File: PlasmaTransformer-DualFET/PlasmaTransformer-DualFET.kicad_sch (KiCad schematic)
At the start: 51 parts, among them J1 Barrel_Jack_MountingPin, J10 Screw_Terminal_01x01, J11 Screw_Terminal_01x01, J12 Screw_Terminal_01x01, J2 Conn_01x02_Pin, J3 Conn_Coaxial, J4 Conn_02x04_Odd_Even, J5 Conn_Coaxial, J6 Screw_Terminal_01x01, J7 Screw_Terminal_01x01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

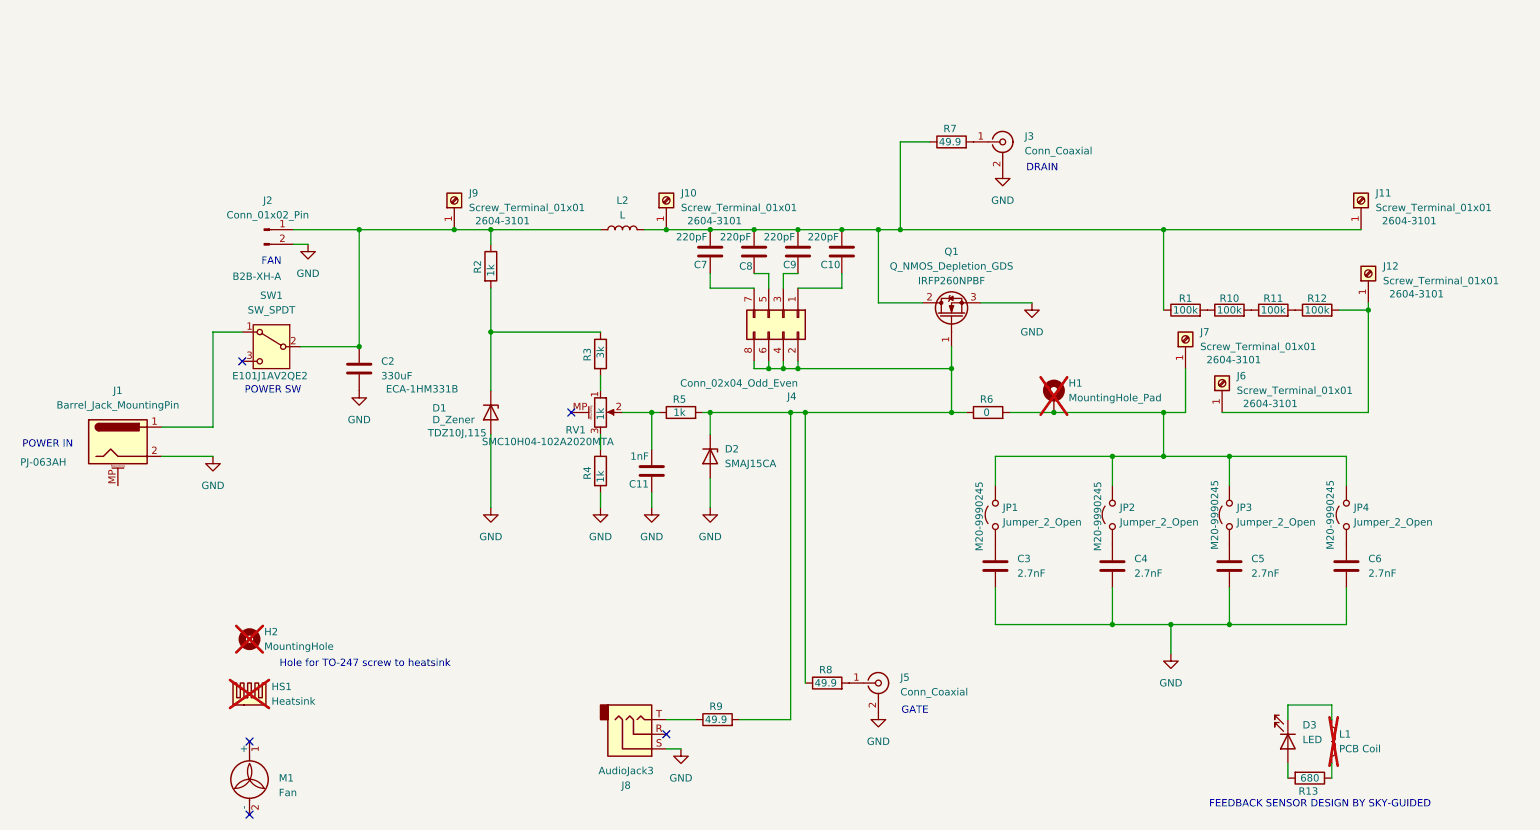
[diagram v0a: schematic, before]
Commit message: Updated rev 2 design and manufacturing files.  Note BOM is not up to date.
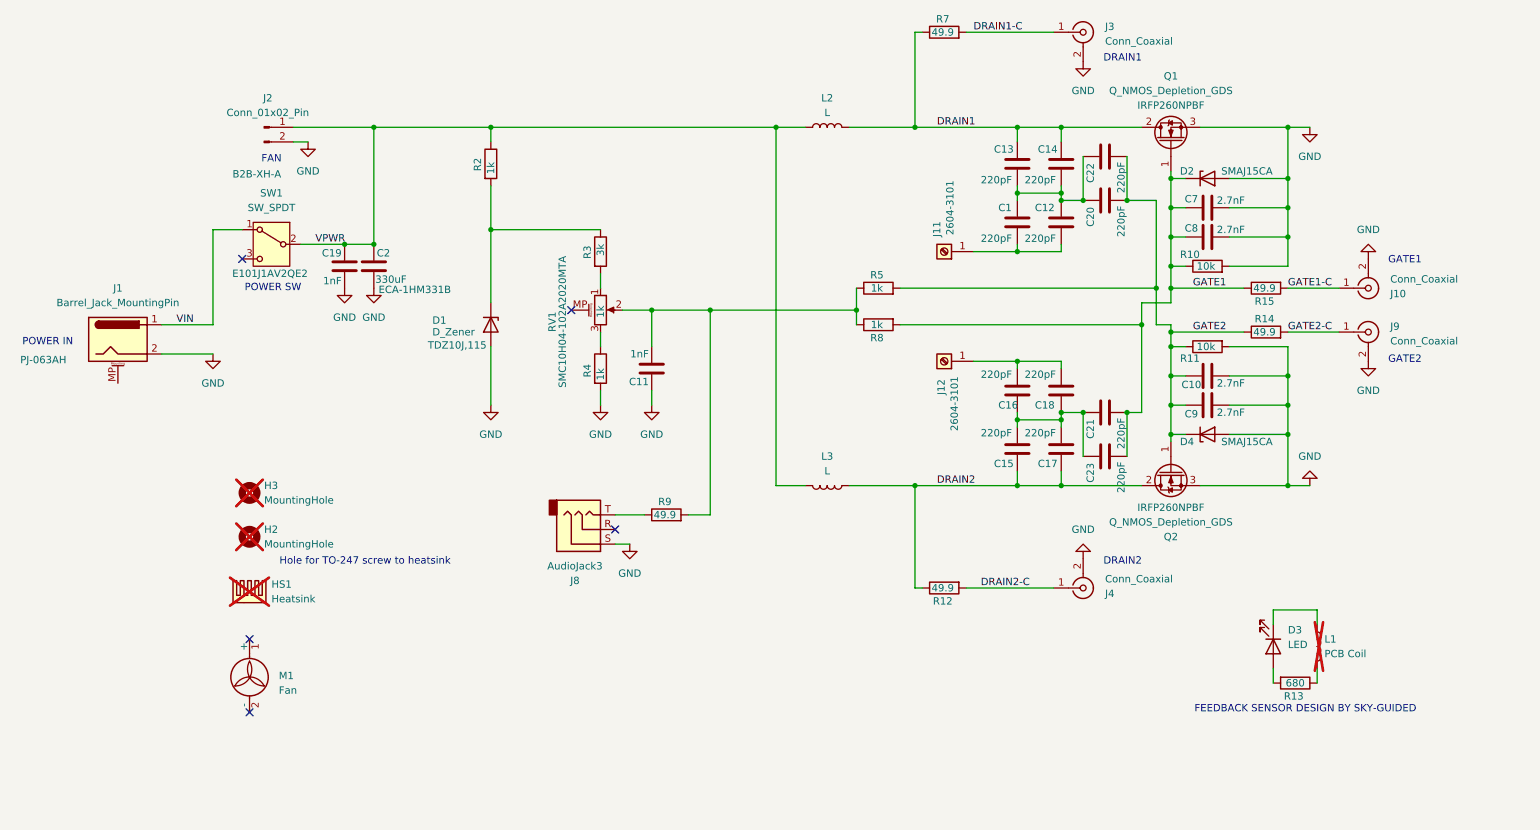
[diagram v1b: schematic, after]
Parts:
- removed C3, C4, C5, C6: 2.7nF, Capacitor_SMD:C_1812_4532Metric, symbol Device:C
- removed H1: MountingHole_Pad, MountingHole:MountingHole_5.3mm_M5_Pad, symbol Mechanical:MountingHole_Pad
- removed J10, J6, J7, J9: Screw_Terminal_01x01, Library:CONN_2604-3101_WAG, symbol Connector:Screw_Terminal_01x01
- removed J4: Conn_02x04_Odd_Even, Connector_PinHeader_2.54mm:PinHeader_2x04_P2.54mm_Vertical, symbol Connector_Generic:Conn_02x04_Odd_Even
- removed J5: Conn_Coaxial, Connector_Coaxial:SMA_Amphenol_901-143_Horizontal, symbol Connector:Conn_Coaxial
- removed JP1, JP2, JP3, JP4: Jumper_2_Open, Connector_PinHeader_2.54mm:PinHeader_1x02_P2.54mm_Vertical, symbol Jumper:Jumper_2_Open
- removed R1: 100k, Resistor_SMD:R_1812_4532Metric, symbol Device:R
- removed R6: 0, Resistor_SMD:R_1812_4532Metric, symbol Device:R
- added C1, C12, C13, C14, C15, C16, C17, C18, C20, C21, C22, C23: 220pF, Capacitor_THT:C_Disc_D10.5mm_W5.0mm_P10.00mm, symbol Device:C
- added C19: 1nF, Capacitor_SMD:C_1812_4532Metric, symbol Device:C
- added D4: SMAJ15CA, Diode_SMD:D_SMC, symbol Device:D_Zener
- added H3: MountingHole, MountingHole:MountingHole_8.4mm_M8, symbol Mechanical:MountingHole
- added J10, J4, J9: Conn_Coaxial, Connector_Coaxial:SMA_Amphenol_901-144_Vertical, symbol Connector:Conn_Coaxial
- added L3: L, Inductor_SMD:L_APV_APH1770, symbol Device:L
- added Q2: Q_NMOS_Depletion_GDS, Package_TO_SOT_THT:TO-247-3_Horizontal_TabDown, symbol Transistor_FET_Other:Q_NMOS_Depletion_GDS
- added R14, R15: 49.9, Resistor_SMD:R_0805_2012Metric, symbol Device:R
- C10, C7, C8, C9: value 220pF -> 2.7nF; MPN CC1812JKNPOCBN221 -> 1812GC272KAT1A; Manufacturer Yageo -> Kyocera
- J3: footprint Connector_Coaxial:SMA_Amphenol_901-143_Horizontal -> Connector_Coaxial:SMA_Amphenol_901-144_Vertical
- R10, R11: value 100k -> 10k; footprint Resistor_SMD:R_1812_4532Metric -> Resistor_SMD:R_0805_2012Metric; MPN ERJ-12NF1003U -> RC0805FR-071KL; Manufacturer Panasonic -> Yageo
- R12: value 100k -> 49.9; footprint Resistor_SMD:R_1812_4532Metric -> Resistor_SMD:R_0805_2012Metric; MPN ERJ-12NF1003U -> RC0805FR-0749R9L; Manufacturer Panasonic -> Yageo
- R8: value 49.9 -> 1k; MPN RC0805FR-0749R9L -> RC0805FR-071KL
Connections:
- net GND: now also C10.2, C7.2, C8.2, C9.2, R10.2, R11.2, C19.1, D4.2 (A), J10.2 (Ext), J4.2 (Ext), J9.2 (Ext), Q2.3 (S)
- net at C11.2, R5.1, RV1.2: now also R8.1, R9.2
- net DRAIN2: now reaches R12.1
- net DRAIN2: now also C15.1, C17.1, L3.1, Q2.2 (D); no longer R11.2
- net at J12.1 (Pin_1): now also C16.2, C18.2; no longer R12.2
- net VPWR: now reaches C2.1, J2.1 (Pin_1), L2.1, R2.1, SW1.2 (B)
- net VPWR: now also C19.2, L3.2
- net GATE2: now reaches C10.1
- net GATE2: now also C9.1, R11.1, R5.2, C20.2, C22.2, D4.1 (K), Q2.1 (G), R14.1
- net GATE1: now reaches C8.1
- net GATE1: now also C7.1, D2.1 (K), Q1.1 (G), R10.1, R8.2, C21.2, C23.2, R15.1
- net DRAIN1-C: now reaches J3.1 (In), R7.2
- net VIN: now reaches J1.1, SW1.1 (A)
- new net: C1.1, C12.1, C13.2, C14.2, C20.1, C22.1
- new net: C1.2, C12.2, J11.1 (Pin_1)
- new net: C15.2, C16.1, C17.2, C18.1, C21.1, C23.1
- new net DRAIN1: C13.1, C14.1, L2.2, Q1.2 (D), R7.1
- new net DRAIN2-C: J4.1 (In), R12.2
- new net GATE1-C: J10.1 (In), R15.2
- new net GATE2-C: J9.1 (In), R14.2
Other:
- note added: "DRAIN1"
- note added: "DRAIN2"
- note added: "GATE1"
- note added: "GATE2"
- note removed: "DRAIN"
- note removed: "GATE"
- moved on the sheet: C11, C2, D1, D2, D3, H2, HS1, J1, J11, J12, J2, J3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
